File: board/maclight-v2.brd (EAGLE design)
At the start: 103.9 x 16 mm, 28 parts, among them IC1 AT90S2313S, U2 STP16CP05SO-24

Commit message: Reving board layout
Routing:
- net GND: track 56.7 -> 55.8 mm
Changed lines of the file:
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@@
 <wire x1="103.886" y1="16.002" x2="0" y2="16.002" width="0" layer="20"/>
 <wire x1="0" y1="16.002" x2="0" y2="0" width="0" layer="20"/>
+<rectangle x1="15.24" y1="9.652" x2="16.764" y2="11.176" layer="1"/>
+<rectangle x1="6.604" y1="3.556" x2="8.128" y2="5.08" layer="1"/>
 </plain>
 <attributes>
@@
 <wire x1="16.51" y1="8.52" x2="16.51" y2="11.938" width="0.4064" layer="1"/>
 <contactref element="U$1" pad="1"/>
-<wire x1="36.576" y1="12.7" x2="42.545" y2="12.7" width="0.254" layer="1"/>
-<wire x1="20.32" y1="13.2842" x2="20.32" y2="11.684" width="0.254" layer="1"/>
-<wire x1="20.32" y1="11.684" x2="21.336" y2="10.668" width="0.254" layer="1"/>
-<wire x1="3.81" y1="5.08" x2="6.096" y2="5.08" width="0.254" layer="1"/>
-<wire x1="6.096" y1="5.08" x2="7.62" y2="3.556" width="0.254" layer="1"/>
-<wire x1="7.62" y1="2.032" x2="7.62" y2="3.556" width="0.254" layer="1"/>
-<wire x1="7.62" y1="3.556" x2="8.636" y2="4.572" width="0.254" layer="1"/>
-<wire x1="8.636" y1="4.572" x2="9.982" y2="4.572" width="0.254" layer="1"/>
-<wire x1="9.982" y1="4.572" x2="10.16" y2="4.75" width="0.254" layer="1"/>
-<wire x1="10.16" y1="4.75" x2="13.538" y2="4.75" width="0.254" layer="1"/>
-<wire x1="13.538" y1="4.75" x2="14.732" y2="3.556" width="0.254" layer="1"/>
-<wire x1="14.732" y1="3.556" x2="16.88" y2="3.556" width="0.254" layer="1"/>
-<wire x1="36.576" y1="12.7" x2="35.052" y2="11.176" width="0.254" layer="1"/>
-<wire x1="35.052" y1="11.176" x2="35.052" y2="10.668" width="0.254" layer="1"/>
-<wire x1="35.052" y1="10.668" x2="35.052" y2="8.774" width="0.254" layer="1"/>
-<wire x1="35.052" y1="8.774" x2="34.925" y2="8.647" width="0.254" layer="1"/>
-<wire x1="21.336" y1="10.668" x2="35.052" y2="10.668" width="0.254" layer="1"/>
-<wire x1="13.538" y1="4.75" x2="16.51" y2="8.52" width="0" layer="19" extent="1-1"/>
+<wire x1="16.88" y1="3.556" x2="16.256" y2="3.556" width="0.4064" layer="1"/>
+<wire x1="16.256" y1="3.556" x2="15.24" y2="4.572" width="0.4064" layer="1"/>
+<wire x1="15.24" y1="4.572" x2="10.338" y2="4.572" width="0.4064" layer="1"/>
+<wire x1="20.32" y1="13.2842" x2="20.32" y2="11.684" width="0.4064" layer="1"/>
+<wire x1="20.32" y1="11.684" x2="21.336" y2="10.668" width="0.4064" layer="1"/>
+<wire x1="21.336" y1="10.668" x2="35.052" y2="10.668" width="0.4064" layer="1"/>
+<wire x1="35.052" y1="10.668" x2="35.052" y2="11.684" width="0.4064" layer="1"/>
+<wire x1="35.052" y1="11.684" x2="36.068" y2="12.7" width="0.4064" layer="1"/>
+<wire x1="36.068" y1="12.7" x2="42.545" y2="12.7" width="0.4064" layer="1"/>
+<wire x1="35.052" y1="10.668" x2="35.052" y2="8.774" width="0.4064" layer="1"/>
+<wire x1="35.052" y1="8.774" x2="34.925" y2="8.647" width="0.4064" layer="1"/>
+<wire x1="3.81" y1="5.08" x2="6.096" y2="5.08" width="0.6096" layer="1"/>
+<wire x1="6.096" y1="5.08" x2="7.62" y2="3.556" width="0.6096" layer="1"/>
+<wire x1="7.62" y1="3.556" x2="7.62" y2="2.032" width="0.6096" layer="1"/>
+<wire x1="7.62" y1="3.556" x2="8.636" y2="4.572" width="0.6096" layer="1"/>
+<wire x1="8.636" y1="4.572" x2="9.982" y2="4.572" width="0.6096" layer="1"/>
+<wire x1="9.982" y1="4.572" x2="10.16" y2="4.75" width="0.6096" layer="1"/>
+<wire x1="15.24" y1="4.572" x2="16.51" y2="8.52" width="0" layer="19" extent="1-1"/>
+<wire x1="10.16" y1="4.75" x2="10.338" y2="4.572" width="0.6096" layer="1"/>
 </signal>
 <signal name="GND">
@@
 <contactref element="IC1" pad="10"/>
 <contactref element="U$1" pad="2"/>
-<wire x1="38.671" y1="6.847" x2="40.643" y2="6.855" width="0.254" layer="1"/>
-<wire x1="40.643" y1="6.855" x2="42.545" y2="4.953" width="0.254" layer="1"/>
-<wire x1="42.545" y1="4.953" x2="42.545" y2="2.54" width="0.254" layer="1"/>
-<wire x1="34.925" y1="6.847" x2="38.671" y2="6.847" width="0.254" layer="1"/>
-<wire x1="31.75" y1="3.7592" x2="33.7312" y2="3.7592" width="0.254" layer="1"/>
-<wire x1="33.7312" y1="3.7592" x2="35.052" y2="5.08" width="0.254" layer="1"/>
-<wire x1="35.052" y1="5.08" x2="35.052" y2="6.728" width="0.254" layer="1"/>
 <wire x1="35.052" y1="6.728" x2="34.925" y2="6.847" width="0.254" layer="1"/>
-<wire x1="31.75" y1="3.7592" x2="31.75" y2="5.842" width="0.254" layer="1"/>
-<wire x1="31.75" y1="5.842" x2="30.988" y2="6.604" width="0.254" layer="1"/>
-<wire x1="30.988" y1="6.604" x2="16.394" y2="6.604" width="0.254" layer="1"/>
 <wire x1="16.307" y1="6.604" x2="16.51" y2="6.72" width="0.254" layer="1"/>
 <contactref element="DGND" pad="1"/>
-<wire x1="3.81" y1="6.58" x2="6.072" y2="6.58" width="0.254" layer="1"/>
-<wire x1="6.072" y1="6.58" x2="7.62" y2="8.128" width="0.254" layer="1"/>
-<wire x1="7.62" y1="8.128" x2="9.982" y2="8.128" width="0.254" layer="1"/>
-<wire x1="9.982" y1="8.128" x2="10.16" y2="7.95" width="0.254" layer="1"/>
-<wire x1="4.064" y1="2.032" x2="2.54" y2="2.032" width="0.254" layer="1"/>
-<wire x1="2.54" y1="2.032" x2="1.524" y2="3.048" width="0.254" layer="1"/>
-<wire x1="1.524" y1="3.048" x2="1.524" y2="5.588" width="0.254" layer="1"/>
-<wire x1="1.524" y1="5.588" x2="2.54" y2="6.604" width="0.254" layer="1"/>
-<wire x1="2.54" y1="6.604" x2="3.786" y2="6.604" width="0.254" layer="1"/>
 <wire x1="3.786" y1="6.604" x2="3.81" y2="6.58" width="0.254" layer="1"/>
-<wire x1="10.16" y1="7.95" x2="13.386" y2="7.95" width="0.254" layer="1"/>
-<wire x1="13.386" y1="7.95" x2="14.732" y2="6.604" width="0.254" layer="1"/>
-<wire x1="14.732" y1="6.604" x2="16.307" y2="6.604" width="0.254" layer="1"/>
 <wire x1="16.307" y1="6.604" x2="16.394" y2="6.604" width="0.254" layer="1"/>
 <wire x1="16.394" y1="6.604" x2="16.51" y2="6.72" width="0.254" layer="1"/>
+<wire x1="42.545" y1="2.54" x2="42.545" y2="4.699" width="0.6096" layer="1"/>
+<wire x1="42.545" y1="4.699" x2="40.64" y2="6.604" width="0.6096" layer="1"/>
+<wire x1="40.64" y1="6.604" x2="38.862" y2="6.604" width="0.6096" layer="1"/>
+<wire x1="38.862" y1="6.604" x2="34.798" y2="6.604" width="0.6096" layer="1"/>
+<wire x1="34.798" y1="6.604" x2="31.75" y2="6.604" width="0.6096" layer="1"/>
+<wire x1="31.75" y1="6.604" x2="16.626" y2="6.604" width="0.6096" layer="1"/>
+<wire x1="16.626" y1="6.604" x2="16.51" y2="6.72" width="0.6096" layer="1"/>
+<wire x1="31.75" y1="3.7592" x2="31.75" y2="6.604" width="0.6096" layer="1"/>
+<wire x1="34.925" y1="6.847" x2="34.798" y2="6.847" width="0.6096" layer="1"/>
+<wire x1="34.798" y1="6.847" x2="34.798" y2="6.604" width="0.6096" layer="1"/>
+<wire x1="38.671" y1="6.847" x2="38.862" y2="6.847" width="0.6096" layer="1"/>
+<wire x1="38.862" y1="6.847" x2="38.862" y2="6.604" width="0.6096" layer="1"/>
+<wire x1="3.81" y1="6.58" x2="6.072" y2="6.58" width="0.6096" layer="1"/>
+<wire x1="6.072" y1="6.58" x2="7.62" y2="8.128" width="0.6096" layer="1"/>
+<wire x1="7.62" y1="8.128" x2="9.982" y2="8.128" width="0.6096" layer="1"/>
+<wire x1="9.982" y1="8.128" x2="10.16" y2="7.95" width="0.6096" layer="1"/>
+<wire x1="16.307" y1="6.604" x2="14.732" y2="6.604" width="0.6096" layer="1"/>
+<wire x1="14.732" y1="6.604" x2="13.208" y2="8.128" width="0.6096" layer="1"/>
+<wire x1="13.208" y1="8.128" x2="10.338" y2="8.128" width="0.6096" layer="1"/>
+<wire x1="10.338" y1="8.128" x2="10.16" y2="7.95" width="0.6096" layer="1"/>
+<wire x1="3.81" y1="6.58" x2="2.008" y2="6.58" width="0.6096" layer="1"/>
+<wire x1="2.008" y1="6.58" x2="1.524" y2="6.096" width="0.6096" layer="1"/>
+<wire x1="1.524" y1="6.096" x2="1.524" y2="3.048" width="0.6096" layer="1"/>
+<wire x1="1.524" y1="3.048" x2="2.54" y2="2.032" width="0.6096" layer="1"/>
+<wire x1="2.54" y1="2.032" x2="4.064" y2="2.032" width="0.6096" layer="1"/>
 </signal>
 <signal name="RESET">

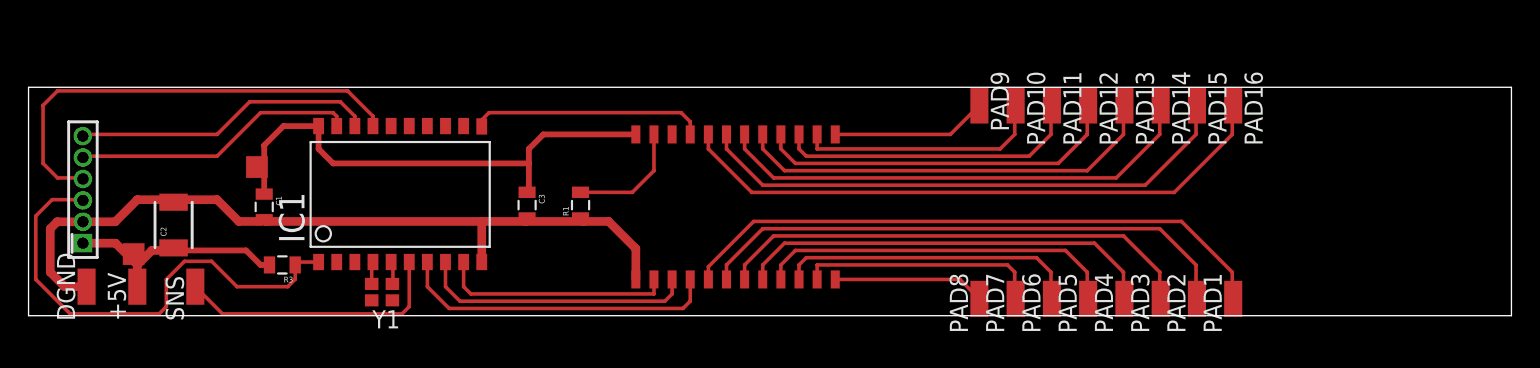
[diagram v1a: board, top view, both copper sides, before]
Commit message: Trying out attiny85 version
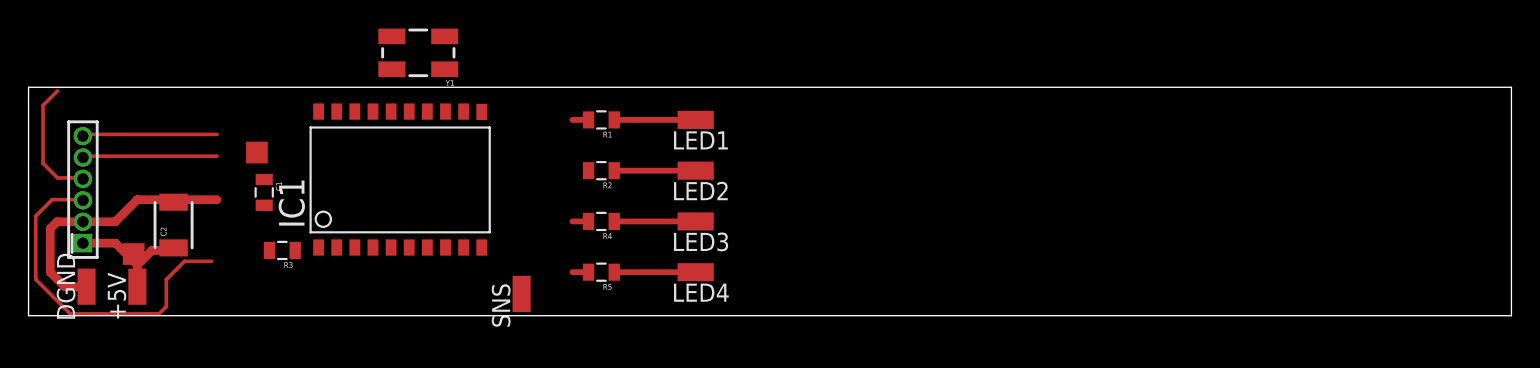
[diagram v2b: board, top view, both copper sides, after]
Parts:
- removed C3: 0.1uF, SparkFun:0805
- removed PAD1, PAD10, PAD11, PAD12, PAD13, PAD14, PAD15, PAD16, PAD2, PAD3, PAD4, PAD5, PAD6, PAD7, PAD8, PAD9: (no value), wirepad:SMD1,27-2,54
- removed U2: STP16CP05SO-24, Synapseware:SO-24
- added LED1, LED2, LED3, LED4: (no value), wirepad:SMD1,27-2,54
- added R2, R4, R5: 68, SparkFun:0805
- R1: value (none) -> 68
- Y1: device crystal:FA-128 -> SparkFun-FreqCtrl:CRYSTAL-SMD-5X3
- moved SNS 22.9 mm to (34.5, 1.52)
- moved Y1 17.0 mm to (27.3, 18.4)
- moved R1 6.15 mm to (40.1, 13.7), turned to 180 degrees
- moved IC1 1.02 mm to (25.4, 9.91)
- moved R3 1.02 mm to (17.8, 4.57)
- moved C1 1.02 mm to (16.5, 8.64)
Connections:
- net RXD renamed RX
- net TXD renamed TX
- removed net N$11: PAD7.1, U2.11
- removed net N$13: PAD8.1, U2.12
- removed net N$14: PAD9.1, U2.13
- removed net N$15: PAD10.1, U2.14
- removed net N$16: PAD11.1, U2.15
- removed net N$17: PAD12.1, U2.16
- removed net N$18: PAD13.1, U2.17
- removed net N$19: PAD14.1, U2.18
- removed net N$20: PAD15.1, U2.19
- removed net N$21: PAD16.1, U2.20
- removed net N$37: PAD5.1, U2.9
- removed net N$5: PAD2.1, U2.6
- removed net N$6: PAD3.1, U2.7
- removed net N$7: PAD4.1, U2.8
- removed net N$8: PAD6.1, U2.10
- new net LED1: IC1.12, R1.2
- new net LED2: IC1.13, R2.2
- new net LED3: IC1.14, R4.2
- new net LED4: IC1.15, R5.2
- new net N$2: LED3.1, R4.1
- new net N$3: LED2.1, R2.1
- net /OE: no longer U2.21
- net 5V: no longer C3.1, U2.24
- net CLK: no longer U2.3
- net DATA: no longer U2.2
- net GND: no longer C3.2, R1.1, U2.1
- net LE: no longer U2.4
- net N$1: now also LED4.1, R5.1; no longer R1.2, U2.23
- net N$12: now also Y1.3; no longer Y1.2
- net N$4: now also LED1.1, R1.1; no longer PAD1.1, U2.5
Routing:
- net N$21: track 42.7 -> 0.00 mm
- net 5V: track 51.8 -> 9.25 mm
- net N$20: track 38.5 -> 0.00 mm
- net N$5: track 38.4 -> 0.00 mm
- net GND: track 55.8 -> 18.7 mm
- net N$4: track 42.3 -> 5.70 mm
- net N$19: track 34.3 -> 0.00 mm
- net N$6: track 33.9 -> 0.00 mm
- net N$18: track 30.0 -> 0.00 mm
- net N$7: track 29.7 -> 0.00 mm
- net N$17: track 25.8 -> 0.00 mm
- net N$37: track 25.4 -> 0.00 mm
- net MOSI/SDA: track 32.3 -> 8.75 mm
- net LE: track 22.5 -> 0.00 mm
- net N$16: track 21.6 -> 0.00 mm
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
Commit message: Working on neopixel + attiny85.  It's not going very well.
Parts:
- moved Y1 12.6 mm to (22.5, 6.73), turned to 90 degrees
- moved LED1 10.7 mm to (46.7, 3.05)
- moved LED4 10.7 mm to (46.7, 13.7)
- moved R1 10.7 mm to (40.1, 3.05)
- moved R5 10.7 mm to (40.1, 13.7)
- moved IC1 5.39 mm to (30.7, 9.14), turned to 270 degrees
- moved LED2 3.56 mm to (46.7, 6.60)
- moved LED3 3.56 mm to (46.7, 10.2)
- moved R2 3.56 mm to (40.1, 6.60)
- moved R4 3.56 mm to (40.1, 10.2)
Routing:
- net LED4: track 1.13 -> 9.20 mm
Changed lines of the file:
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@@
 <element name="C2" library="SparkFun" package="1210" value="10uF" x="10.16" y="6.35" rot="R90"/>
 <element name="R3" library="SparkFun" package="0805" value="1k" x="17.78" y="4.572" rot="R180"/>
-<element name="IC1" library="atmel" package="SO20L" value="AT90S2313S" x="25.4" y="9.906">
-<attribute name="MF" value="" x="25.4" y="9.906" size="1.778" layer="27" display="off"/>
-<attribute name="MPN" value="" x="25.4" y="9.906" size="1.778" layer="27" display="off"/>
-<attribute name="OC_FARNELL" value="unknown" x="25.4" y="9.906" size="1.778" layer="27" display="off"/>
-<attribute name="OC_NEWARK" value="unknown" x="25.4" y="9.906" size="1.778" layer="27" display="off"/>
+<element name="IC1" library="atmel" package="SO20L" value="AT90S2313S" x="30.734" y="9.144" rot="R270">
+<attribute name="MF" value="" x="30.734" y="9.144" size="1.778" layer="27" rot="R270" display="off"/>
+<attribute name="MPN" value="" x="30.734" y="9.144" size="1.778" layer="27" rot="R270" display="off"/>
+<attribute name="OC_FARNELL" value="unknown" x="30.734" y="9.144" size="1.778" layer="27" rot="R270" display="off"/>
+<attribute name="OC_NEWARK" value="unknown" x="30.734" y="9.144" size="1.778" layer="27" rot="R270" display="off"/>
 </element>
-<element name="Y1" library="SparkFun-FreqCtrl" package="CRYSTAL-SMD-5X3" value="" x="27.305" y="18.415" rot="R180"/>
+<element name="Y1" library="SparkFun-FreqCtrl" package="CRYSTAL-SMD-5X3" value="" x="22.479" y="6.731" rot="R90"/>
 <element name="+5V" library="wirepad" package="SMD1,27-2,54" value="" x="7.62" y="2.032"/>
 <element name="U$1" library="SparkFun-Connectors" package="AVR_MINI_PROG" value="AVR_MINI_PROGSMD" x="3.81" y="5.08" rot="R90"/>
 <element name="SNS" library="wirepad" package="SMD1,27-2,54" value="" x="34.544" y="1.524"/>
 <element name="DGND" library="wirepad" package="SMD1,27-2,54" value="" x="4.064" y="2.032"/>
-<element name="R1" library="SparkFun" package="0805" value="68" x="40.132" y="13.716" rot="R180"/>
-<element name="R2" library="SparkFun" package="0805" value="68" x="40.132" y="10.16" rot="R180"/>
-<element name="R4" library="SparkFun" package="0805" value="68" x="40.132" y="6.604" rot="R180"/>
-<element name="R5" library="SparkFun" package="0805" value="68" x="40.132" y="3.048" rot="R180"/>
-<element name="LED1" library="wirepad" package="SMD1,27-2,54" value="" x="46.736" y="13.716" rot="R90"/>
-<element name="LED2" library="wirepad" package="SMD1,27-2,54" value="" x="46.736" y="10.16" rot="R90"/>
-<element name="LED3" library="wirepad" package="SMD1,27-2,54" value="" x="46.736" y="6.604" rot="R90"/>
-<element name="LED4" library="wirepad" package="SMD1,27-2,54" value="" x="46.736" y="3.048" rot="R90"/>
+<element name="R1" library="SparkFun" package="0805" value="68" x="40.132" y="3.048" rot="R180"/>
+<element name="R2" library="SparkFun" package="0805" value="68" x="40.132" y="6.604" rot="R180"/>
+<element name="R4" library="SparkFun" package="0805" value="68" x="40.132" y="10.16" rot="R180"/>
+<element name="R5" library="SparkFun" package="0805" value="68" x="40.132" y="13.716" rot="R180"/>
+<element name="LED1" library="wirepad" package="SMD1,27-2,54" value="" x="46.736" y="3.048" rot="R90"/>
+<element name="LED2" library="wirepad" package="SMD1,27-2,54" value="" x="46.736" y="6.604" rot="R90"/>
+<element name="LED3" library="wirepad" package="SMD1,27-2,54" value="" x="46.736" y="10.16" rot="R90"/>
+<element name="LED4" library="wirepad" package="SMD1,27-2,54" value="" x="46.736" y="13.716" rot="R90"/>
 </elements>
 <signals>
@@
 <wire x1="9.982" y1="4.572" x2="10.16" y2="4.75" width="0.6096" layer="1"/>
 <wire x1="10.16" y1="4.75" x2="10.338" y2="4.572" width="0.6096" layer="1"/>
-<wire x1="16.51" y1="9.536" x2="20.32" y2="14.3002" width="0" layer="19" extent="1-1"/>
+<wire x1="16.51" y1="9.536" x2="35.1282" y2="14.224" width="0" layer="19" extent="1-1"/>
 <wire x1="16.88" y1="4.572" x2="16.51" y2="9.536" width="0" layer="19" extent="1-1"/>
 <wire x1="10.338" y1="4.572" x2="16.88" y2="4.572" width="0" layer="19" extent="1-1"/>
@@
 <wire x1="1.524" y1="3.048" x2="2.54" y2="2.032" width="0.6096" layer="1"/>
 <wire x1="2.54" y1="2.032" x2="4.064" y2="2.032" width="0.6096" layer="1"/>
-<wire x1="16.51" y1="7.736" x2="31.75" y2="4.7752" width="0" layer="19" extent="1-1"/>
+<wire x1="16.51" y1="7.736" x2="25.6032" y2="2.794" width="0" layer="19" extent="1-1"/>
 <wire x1="13.208" y1="8.128" x2="16.51" y2="7.736" width="0" layer="19" extent="1-1"/>
 </signal>
@@
 <wire x1="1.651" y1="8.128" x2="3.762" y2="8.128" width="0.254" layer="1"/>
 <wire x1="3.762" y1="8.128" x2="3.81" y2="8.08" width="0.254" layer="1"/>
-<wire x1="18.68" y1="4.572" x2="20.32" y2="4.7752" width="0" layer="19" extent="1-1"/>
+<wire x1="18.68" y1="4.572" x2="25.6032" y2="14.224" width="0" layer="19" extent="1-1"/>
 <wire x1="12.827" y1="3.81" x2="18.68" y2="4.572" width="0" layer="19" extent="1-1"/>
 </signal>
@@
 <wire x1="13.208" y1="12.7" x2="3.92" y2="12.7" width="0.254" layer="1"/>
 <wire x1="3.92" y1="12.7" x2="3.8" y2="12.58" width="0.254" layer="1"/>
-<wire x1="13.208" y1="12.7" x2="22.86" y2="14.3002" width="0" layer="19" extent="1-1"/>
+<wire x1="13.208" y1="12.7" x2="35.1282" y2="11.684" width="0" layer="19" extent="1-1"/>
 </signal>
 <signal name="DATA">
@@
 <wire x1="13.208" y1="11.176" x2="3.906" y2="11.176" width="0.254" layer="1"/>
 <wire x1="3.906" y1="11.176" x2="3.81" y2="11.08" width="0.254" layer="1"/>
-<wire x1="13.208" y1="11.176" x2="21.59" y2="14.3002" width="0" layer="19" extent="1-1"/>
+<wire x1="13.208" y1="11.176" x2="35.1282" y2="12.954" width="0" layer="19" extent="1-1"/>
 </signal>
 <signal name="MOSI/SDA">
@@
 <wire x1="2.032" y1="9.652" x2="3.738" y2="9.652" width="0.254" layer="1"/>
 <wire x1="3.738" y1="9.652" x2="3.81" y2="9.58" width="0.254" layer="1"/>
-<wire x1="3.81" y1="9.58" x2="24.13" y2="14.3002" width="0" layer="19" extent="1-1"/>
+<wire x1="3.81" y1="9.58" x2="35.1282" y2="10.414" width="0" layer="19" extent="1-1"/>
 </signal>
 <signal name="N$10">
 <contactref element="IC1" pad="5"/>
 <contactref element="Y1" pad="1"/>
-<wire x1="25.4" y1="4.7752" x2="29.155" y2="19.565" width="0" layer="19" extent="1-1"/>
+<wire x1="25.6032" y1="9.144" x2="23.629" y2="4.881" width="0" layer="19" extent="1-1"/>
 </signal>
 <signal name="N$12">
 <contactref element="IC1" pad="4"/>
 <contactref element="Y1" pad="3"/>
-<wire x1="24.13" y1="4.7752" x2="25.455" y2="17.265" width="0" layer="19" extent="1-1"/>
+<wire x1="25.6032" y1="10.414" x2="21.329" y2="8.581" width="0" layer="19" extent="1-1"/>
 </signal>
 <signal name="TX">
@@
 <contactref element="SNS" pad="1"/>
 <contactref element="IC1" pad="6"/>
-<wire x1="26.67" y1="4.7752" x2="34.544" y2="1.524" width="0" layer="19" extent="1-1"/>
+<wire x1="25.6032" y1="7.874" x2="34.544" y2="1.524" width="0" layer="19" extent="1-1"/>
 </signal>
 <signal name="LED1">
 <contactref element="IC1" pad="12"/>
 <contactref element="R1" pad="2"/>
-<wire x1="38.1" y1="13.716" x2="39.232" y2="13.716" width="0.4064" layer="1"/>
-<wire x1="30.48" y1="14.3002" x2="38.1" y2="13.716" width="0" layer="19" extent="1-1"/>
+<wire x1="38.1" y1="3.048" x2="39.232" y2="3.048" width="0.4064" layer="1"/>
+<wire x1="35.1282" y1="4.064" x2="38.1" y2="3.048" width="0" layer="19" extent="1-1"/>
 </signal>
 <signal name="LED2">
 <contactref element="IC1" pad="13"/>
 <contactref element="R2" pad="2"/>
-<wire x1="29.21" y1="14.3002" x2="39.232" y2="10.16" width="0" layer="19" extent="1-1"/>
+<wire x1="35.1282" y1="5.334" x2="39.232" y2="6.604" width="0" layer="19" extent="1-1"/>
 </signal>
 <signal name="LED3">
 <contactref element="IC1" pad="14"/>
 <contactref element="R4" pad="2"/>
-<wire x1="38.1" y1="6.604" x2="39.232" y2="6.604" width="0.4064" layer="1"/>
-<wire x1="27.94" y1="14.3002" x2="38.1" y2="6.604" width="0" layer="19" extent="1-1"/>
+<wire x1="38.1" y1="10.16" x2="39.232" y2="10.16" width="0.4064" layer="1"/>
+<wire x1="35.1282" y1="6.604" x2="38.1" y2="10.16" width="0" layer="19" extent="1-1"/>
 </signal>
 <signal name="LED4">
 <contactref element="IC1" pad="15"/>
 <contactref element="R5" pad="2"/>
-<wire x1="38.1" y1="3.048" x2="39.232" y2="3.048" width="0.4064" layer="1"/>
-<wire x1="26.67" y1="14.3002" x2="38.1" y2="3.048" width="0" layer="19" extent="1-1"/>
+<wire x1="37.592" y1="13.716" x2="39.232" y2="13.716" width="0.4064" layer="1"/>
+<wire x1="35.1282" y1="7.874" x2="36.322" y2="7.874" width="0.4064" layer="1"/>
+<wire x1="36.322" y1="7.874" x2="36.576" y2="8.128" width="0.4064" layer="1"/>
+<wire x1="36.576" y1="8.128" x2="36.576" y2="12.7" width="0.4064" layer="1"/>
+<wire x1="36.576" y1="12.7" x2="37.592" y2="13.716" width="0.4064" layer="1"/>
 </signal>
 <signal name="N$1">
 <contactref element="R5" pad="1"/>
 <contactref element="LED4" pad="1"/>
-<wire x1="41.032" y1="3.048" x2="46.736" y2="3.048" width="0.4064" layer="1"/>
-<wire x1="47.244" y1="3.048" x2="46.736" y2="3.048" width="0.4064" layer="1"/>
+<wire x1="41.032" y1="13.716" x2="46.736" y2="13.716" width="0.4064" layer="1"/>
+<wire x1="47.244" y1="13.716" x2="46.736" y2="13.716" width="0.4064" layer="1"/>
 </signal>
 <signal name="N$2">
 <contactref element="R4" pad="1"/>
 <contactref element="LED3" pad="1"/>
-<wire x1="41.032" y1="6.604" x2="46.736" y2="6.604" width="0.4064" layer="1"/>
+<wire x1="41.032" y1="10.16" x2="46.736" y2="10.16" width="0.4064" layer="1"/>
 </signal>
 <signal name="N$3">
 <contactref element="R2" pad="1"/>
 <contactref element="LED2" pad="1"/>
-<wire x1="41.032" y1="10.16" x2="46.736" y2="10.16" width="0.4064" layer="1"/>
+<wire x1="41.032" y1="6.604" x2="46.736" y2="6.604" width="0.4064" layer="1"/>
 </signal>
 <signal name="N$4">
 <contactref element="R1" pad="1"/>
 <contactref element="LED1" pad="1"/>
-<wire x1="41.032" y1="13.716" x2="46.736" y2="13.716" width="0.4064" layer="1"/>
+<wire x1="41.032" y1="3.048" x2="46.736" y2="3.048" width="0.4064" layer="1"/>
 </signal>
 </signals>
